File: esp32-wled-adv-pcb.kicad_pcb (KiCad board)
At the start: 2 copper layers, 91.5 x 44.5 mm, 50 parts, among them J1 Conn_01x03_Male, J2 Conn_01x03_Male, J4 Screw_Terminal_01x02, J5 Conn_01x02, Q1 BS170F, SW1 SW_Push, SW2 SW_Push, U1 MT3420C, U2 ESP32-PICO-D4

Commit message: change series resistor values for potentiometers
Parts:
- R10, R12, R8: value 4k7 -> 820R
- R11, R13, R9: value 4k7 -> 510R
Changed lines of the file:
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@@
   (net 48 "/LED_DATA")
   (net 49 "Net-(Q1-Pad3)")
-  (net 50 "Net-(R4-Pad2)")
+  (net 50 "Net-(C14-Pad2)")
   (net 51 "Net-(R5-Pad2)")
   (net 52 "Net-(R8-Pad2)")
@@
       (effects (font (size 1 1) (thickness 0.15)) (justify left))
     )
-    (fp_text value "4k7" (at 0 1.65 90) (layer "F.Fab")
+    (fp_text value "510R" (at 0 1.65 90) (layer "F.Fab")
       (effects (font (size 1 1) (thickness 0.15)))
     )
@@
       (effects (font (size 1 1) (thickness 0.15)) (justify right))
     )
-    (fp_text value "4k7" (at 0 1.65 90) (layer "F.Fab")
+    (fp_text value "820R" (at 0 1.65 90) (layer "F.Fab")
       (effects (font (size 1 1) (thickness 0.15)))
     )
@@
       (effects (font (size 1 1) (thickness 0.15)) (justify left))
     )
-    (fp_text value "4k7" (at 0 1.65 90) (layer "F.Fab")
+    (fp_text value "510R" (at 0 1.65 90) (layer "F.Fab")
       (effects (font (size 1 1) (thickness 0.15)))
     )
@@
       (effects (font (size 1 1) (thickness 0.15)) (justify left))
     )
-    (fp_text value "4k7" (at 0 1.65 90) (layer "F.Fab")
+    (fp_text value "510R" (at 0 1.65 90) (layer "F.Fab")
       (effects (font (size 1 1) (thickness 0.15)))
     )
@@
       (effects (font (size 1 1) (thickness 0.15)) (justify right))
     )
-    (fp_text value "4k7" (at 0 1.65 90) (layer "F.Fab")
+    (fp_text value "820R" (at 0 1.65 90) (layer "F.Fab")
       (effects (font (size 1 1) (thickness 0.15)))
     )
@@
     (fp_line (start 1 -0.625) (end 1 0.625) (layer "F.Fab") (width 0.1))
     (pad "1" smd roundrect (at -0.9125 0) (size 1.025 1.4) (layers "F.Cu" "F.Paste" "F.Mask") (roundrect_rratio 0.243902439)
-      (net 50 "Net-(R4-Pad2)") (pintype "passive"))
+      (net 50 "Net-(C14-Pad2)") (pintype "passive"))
     (pad "2" smd roundrect (at 0.9125 0) (size 1.025 1.4) (layers "F.Cu" "F.Paste" "F.Mask") (roundrect_rratio 0.243902439)
       (net 51 "Net-(R5-Pad2)") (pintype "passive"))
@@
       (net 4 "+3V3") (pintype "passive"))
     (pad "2" smd roundrect (at 0.95 0 90) (size 1 1.45) (layers "F.Cu" "F.Paste" "F.Mask") (roundrect_rratio 0.25)
-      (net 50 "Net-(R4-Pad2)") (pintype "passive"))
+      (net 50 "Net-(C14-Pad2)") (pintype "passive"))
     (model "${KICAD6_3DMODEL_DIR}/Capacitor_SMD.3dshapes/C_0805_2012Metric.wrl"
       (offset (xyz 0 0 0))
@@
       (net 4 "+3V3") (pintype "passive"))
     (pad "2" smd roundrect (at 0.9125 0 90) (size 1.025 1.4) (layers "F.Cu" "F.Paste" "F.Mask") (roundrect_rratio 0.243902439)
-      (net 50 "Net-(R4-Pad2)") (pintype "passive"))
+      (net 50 "Net-(C14-Pad2)") (pintype "passive"))
     (model "${KICAD6_3DMODEL_DIR}/Resistor_SMD.3dshapes/R_0805_2012Metric.wrl"
       (offset (xyz 0 0 0))
@@
       (effects (font (size 1 1) (thickness 0.15)) (justify right))
     )
-    (fp_text value "4k7" (at 0 1.65 90) (layer "F.Fab")
+    (fp_text value "820R" (at 0 1.65 90) (layer "F.Fab")
       (effects (font (size 1 1) (thickness 0.15)))
     )
@@
       (net 7 "unconnected-(U1-Pad5)") (pinfunction "NC") (pintype "no_connect"))
     (pad "6" smd roundrect (at 1.1375 -0.95 270) (size 1.325 0.6) (layers "F.Cu" "F.Paste" "F.Mask") (roundrect_rratio 0.25)
-      (net 50 "Net-(R4-Pad2)") (pinfunction "FB") (pintype "input"))
+      (net 50 "Net-(C14-Pad2)") (pinfunction "FB") (pintype "input"))
     (model "${KICAD6_3DMODEL_DIR}/Package_TO_SOT_SMD.3dshapes/SOT-23-6.wrl"
       (offset (xyz 0 0 0))

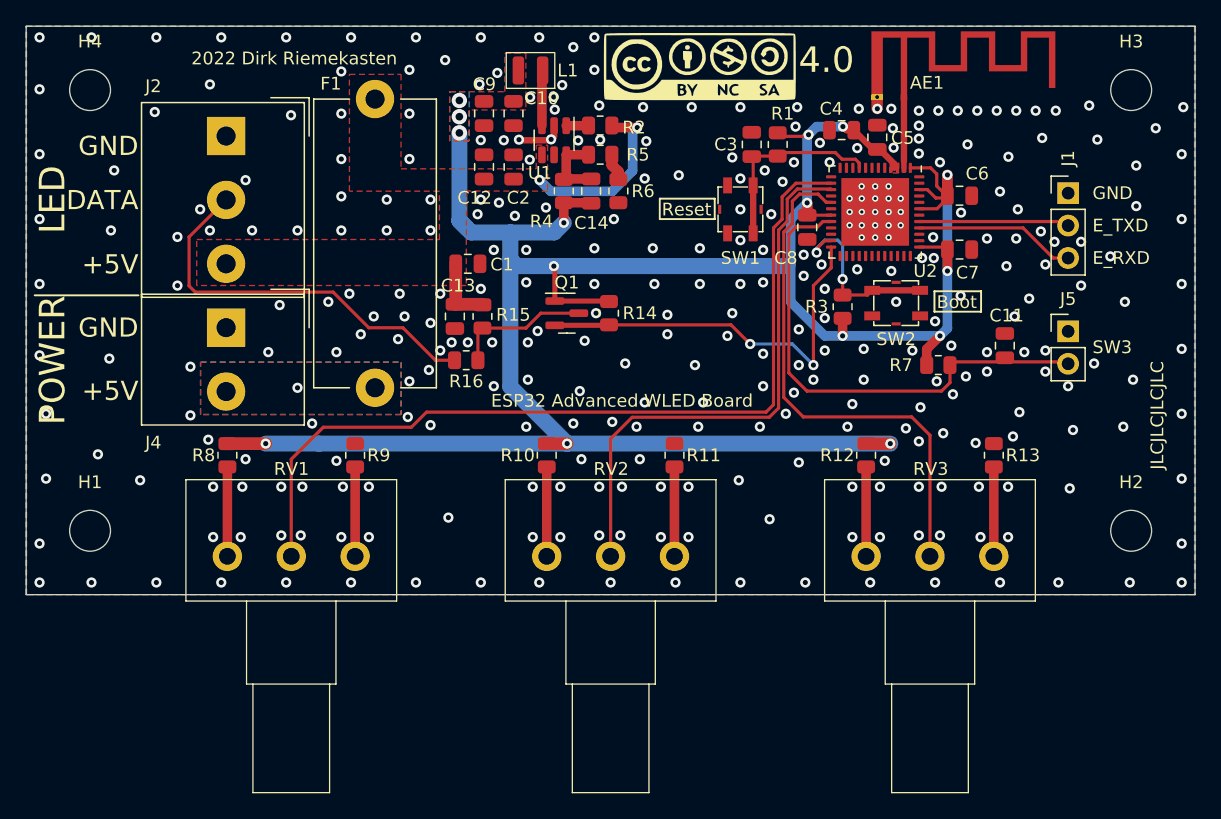
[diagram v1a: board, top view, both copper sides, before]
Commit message: change GPIOs for analog inputs and add a second pushbutton
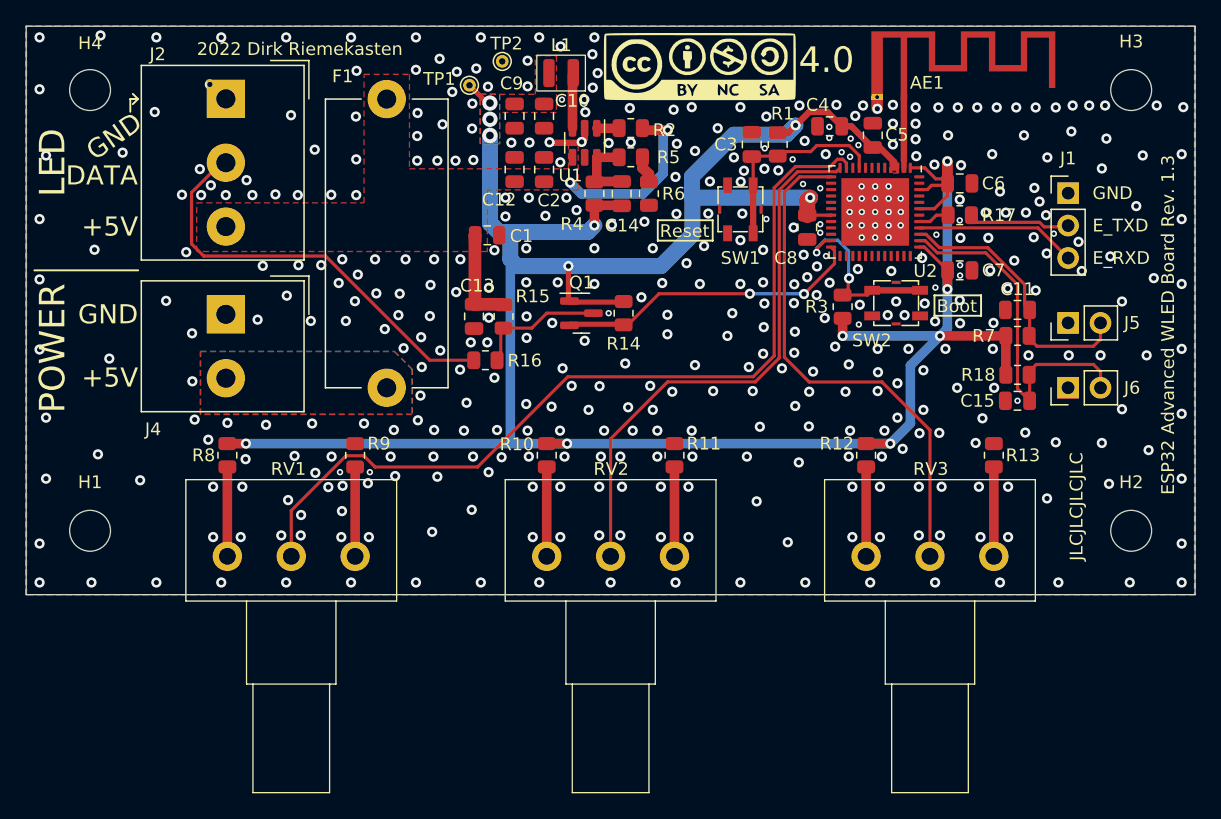
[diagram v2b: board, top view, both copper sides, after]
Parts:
- added C15: 100n, Capacitor_SMD:C_0805_2012Metric, F.Cu at (158.9, 115.8)
- added J6: Conn_01x02, Connector_PinHeader_2.54mm:PinHeader_1x02_P2.54mm_Vertical, F.Cu at (162.8, 114.8)
- added R17: 470R, Resistor_SMD:R_0805_2012Metric, F.Cu at (154.3, 101.3)
- added R18: 4k7, Resistor_SMD:R_0805_2012Metric, F.Cu at (158.9, 113.8)
- added TP1: 3V3, TestPoint:TestPoint_THTPad_D1.0mm_Drill0.5mm, F.Cu at (116.0, 91.1)
- added TP2: GND, TestPoint:TestPoint_THTPad_D1.0mm_Drill0.5mm, F.Cu at (118.5, 89.3)
- moved R7 6.61 mm to (158.9, 110.7)
- moved C11 2.96 mm to (158.9, 108.7), turned to 180 degrees
- moved J2 2.91 mm to (96.9, 92.2)
- moved C1 2.70 mm to (117.3, 102.9)
- moved R6 2.40 mm to (130.0, 99.6)
- moved C12 2.40 mm to (119.5, 97.7)
- moved C10 2.40 mm to (121.8, 93.5)
- moved C2 2.40 mm to (121.8, 97.7)
- moved C9 2.40 mm to (119.5, 93.5)
- moved R2 2.40 mm to (128.6, 94.5)
- moved R5 2.40 mm to (128.6, 96.8)
- moved U1 2.40 mm to (125.0, 95.6)
- moved L1 2.40 mm to (123.1, 90.2)
- moved C14 2.40 mm to (127.9, 99.6)
- moved R4 2.40 mm to (125.7, 99.6)
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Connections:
- C11 pad 1: /WLED_CTRL_IO13 -> /WLED_CTRL_IO22
- J5 pad 2: /WLED_CTRL_IO13 -> /WLED_CTRL_IO22
- R7 pad 2: /WLED_CTRL_IO13 -> /WLED_CTRL_IO22
- RV1 pad 2: /WLED_CTRL_IO25 -> /WLED_CTRL_IO35
- RV2 pad 2: /WLED_CTRL_IO26 -> /WLED_CTRL_IO32
- RV3 pad 2: /WLED_CTRL_IO14 -> /WLED_CTRL_IO33
- U2 pad 11: unconnected-(U2-Pad11) -> /WLED_CTRL_IO35
- U2 pad 12: unconnected-(U2-Pad12) -> /WLED_CTRL_IO32
- U2 pad 13: unconnected-(U2-Pad13) -> /WLED_CTRL_IO33
- U2 pad 14: /WLED_CTRL_IO25 -> unconnected-(U2-Pad14)
- U2 pad 15: /WLED_CTRL_IO26 -> unconnected-(U2-Pad15)
- U2 pad 17: /WLED_CTRL_IO14 -> unconnected-(U2-Pad17)
- U2 pad 20: /WLED_CTRL_IO13 -> unconnected-(U2-Pad20)
- U2 pad 38: unconnected-(U2-Pad38) -> /WLED_CTRL_IO19
- U2 pad 39: unconnected-(U2-Pad39) -> /WLED_CTRL_IO22
- U2 pad 41: /ESP_TXD -> Net-(R17-Pad1)
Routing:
- net /WLED_CTRL_IO25: track 67.9 -> 0.00 mm
- net /WLED_CTRL_IO35: track 0.00 -> 67.4 mm
- net /WLED_CTRL_IO26: track 43.8 -> 0.00 mm
- net /WLED_CTRL_IO32: track 0.00 -> 43.6 mm
- net /WLED_CTRL_IO14: track 41.3 -> 0.00 mm
- net /WLED_CTRL_IO33: track 0.00 -> 40.7 mm
- net /WLED_CTRL_IO13: track 39.1 -> 0.00 mm
- net /WLED_CTRL_IO19: track 0.00 -> 28.2 mm
- net /WLED_CTRL_IO22: track 0.00 -> 21.6 mm
- net +3V3: track 195.8 -> 211.4 mm, vias 15 -> 14
- net Net-(Q1-Pad2): track 31.4 -> 24.2 mm
- net /ESP_TXD: track 11.8 -> 8.08 mm
- net Net-(R17-Pad1): track 0.00 -> 2.46 mm
- net /LED_DATA: track 31.1 -> 33.6 mm
- net +5V: track 19.3 -> 21.6 mm
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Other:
- board text added: "ESP32 Advanced WLED Board Rev. 1.3"
- board text removed: "ESP32 Advanced WLED Board"
- board text removed: "SW3"
